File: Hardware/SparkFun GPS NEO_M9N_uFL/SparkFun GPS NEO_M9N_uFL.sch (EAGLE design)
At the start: 51 parts, among them J13 U.FL, J2 Qwiic Right Angle, J4 Qwiic Right Angle, U1 U-BLOX_NEO-M9N, U2 3.3V

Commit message: Updates both designs with 5.1k resistor in 0603 package
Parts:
- R12, R13: device SparkFun-Resistors:5.1KOHM-0402-1/16W-1% -> SparkFun-Resistors:5.1KOHM5.1KOHM-0603-1/10W-1%
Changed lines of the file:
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@@
 <part name="J5" library="SparkFun-Connectors" deviceset="CONN_04" device="1X04_NO_SILK"/>
 <part name="J3" library="SparkFun-Connectors" deviceset="USB_C" device="2-LAYER"/>
-<part name="R12" library="SparkFun-Resistors" deviceset="5.1KOHM" device="-0402-1/16W-1%" value="5.1k"/>
-<part name="R13" library="SparkFun-Resistors" deviceset="5.1KOHM" device="-0402-1/16W-1%" value="5.1k"/>
+<part name="R12" library="SparkFun-Resistors" deviceset="5.1KOHM" device="5.1KOHM-0603-1/10W-1%" value="5.1k"/>
+<part name="R13" library="SparkFun-Resistors" deviceset="5.1KOHM" device="5.1KOHM-0603-1/10W-1%" value="5.1k"/>
 <part name="GND9" library="SparkFun-PowerSymbols" deviceset="GND" device=""/>
 <part name="GND17" library="SparkFun-PowerSymbols" deviceset="GND" device=""/>

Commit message: Missed version updated
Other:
- note added: "V10"
- note removed: "V01"
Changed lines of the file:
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@@
 <sheet>
 <plain>
-<text x="237.744" y="7.366" size="2.54" layer="94" font="vector">V01</text>
+<text x="237.744" y="7.366" size="2.54" layer="94" font="vector">V10</text>
 <text x="55.88" y="119.38" size="1.778" layer="97" font="vector" align="center">7-bit unshifted I2C address: 0x42</text>
 <wire x1="0" y1="106.68" x2="73.66" y2="106.68" width="0.1524" layer="97" style="shortdash"/>

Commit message: Removes local eagle library and replaces part from that library with part from SparkFun Eagle Library
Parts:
- U1: device gps:U-BLOX_NEO-M9N -> SparkFun-GPS:U-BLOX_NEO-M9N
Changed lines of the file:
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@@
 <?xml version="1.0" encoding="utf-8"?>
 <!DOCTYPE eagle SYSTEM "eagle.dtd">
-<eagle version="9.4.2">
+<eagle version="9.5.1">
 <drawing>
 <settings>
@@
 <part name="SUPPLY11" library="SparkFun-PowerSymbols" deviceset="5V" device=""/>
 <part name="LOGO2" library="SparkFun-Aesthetics" deviceset="SFE_LOGO_NAME_FLAME" device=".1_INCH"/>
-<part name="U1" library="gps" deviceset="U-BLOX_NEO-M9N" device=""/>
+<part name="U1" library="SparkFun-GPS" deviceset="U-BLOX_NEO-M9N" device=""/>
 <part name="PWR\" library="SparkFun-Jumpers" deviceset="JUMPER-SMT_2_NC_TRACE" device="_SILK" value="JUMPER-SMT_2_NC_TRACE_SILK"/>
 <part name="D3" library="SparkFun-IC-Power" deviceset="PRTR5V0U2" device="F"/>

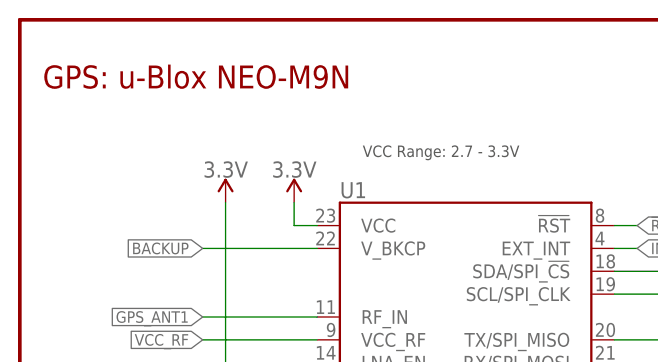
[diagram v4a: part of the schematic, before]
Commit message: Fixes "u-blox" typos in schematic
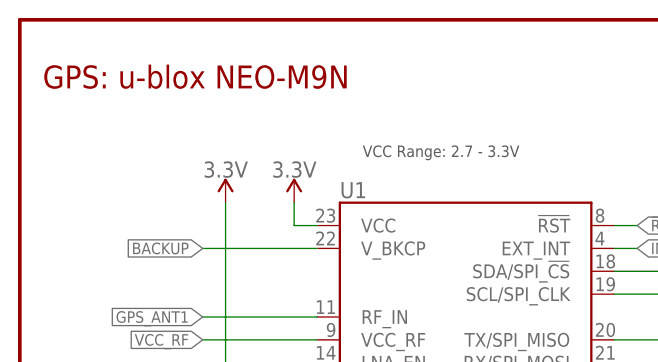
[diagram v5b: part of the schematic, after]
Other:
- note added: "GPS: u-blox NEO-M9N"
- note removed: "GPS: u-Blox NEO-M9N"
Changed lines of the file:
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@@
 <?xml version="1.0" encoding="utf-8"?>
 <!DOCTYPE eagle SYSTEM "eagle.dtd">
-<eagle version="9.5.1">
+<eagle version="9.6.2">
 <drawing>
 <settings>
@@
 <text x="2.54" y="99.06" size="2.54" layer="94" font="vector">LEDs and Jumpers</text>
 <text x="149.86" y="116.84" size="2.54" layer="94" font="vector">Hot Start Battery</text>
-<text x="2.54" y="177.8" size="2.54" layer="94" font="vector">GPS: u-Blox NEO-M9N </text>
+<text x="2.54" y="177.8" size="2.54" layer="94" font="vector">GPS: u-blox NEO-M9N </text>
 <wire x1="73.66" y1="106.68" x2="73.66" y2="0" width="0.1524" layer="97" style="shortdash"/>
 <wire x1="27.94" y1="48.26" x2="27.94" y2="40.64" width="0.2032" layer="97" style="dashdot"/>
